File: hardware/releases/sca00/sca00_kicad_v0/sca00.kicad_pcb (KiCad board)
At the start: 2 copper layers, 91.4 x 33 mm, 37 parts, among them J1 Conn_01x13_Pin, J2 Conn_01x03_Pin, J3 Conn_01x06_Pin, J4 Conn_01x03_Pin, J5 Conn_01x01_Pin, J6 Conn_01x01_Pin, SW1 SW_DIP_x02, SW2 SW_DIP_x02, U1 REF6030, U2 ADS8881, U3 SN74LV4051, U4 THS4281

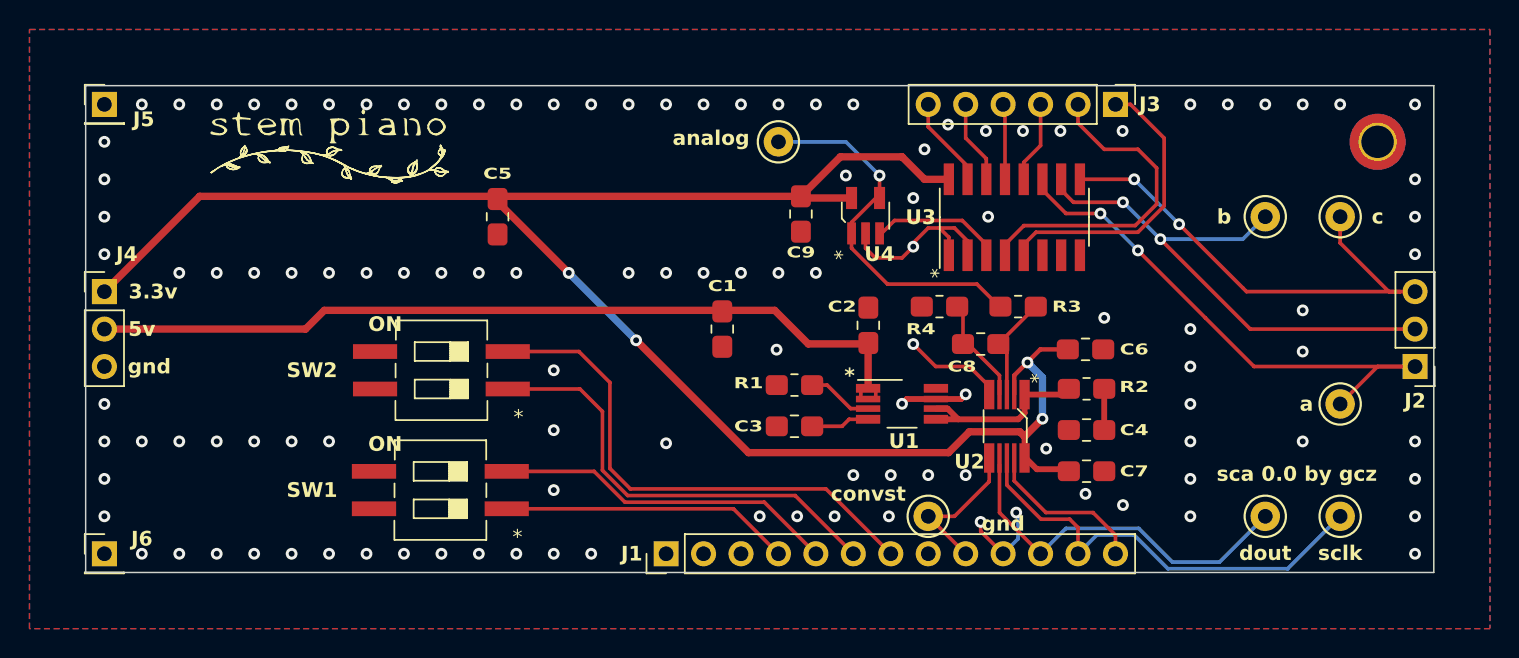
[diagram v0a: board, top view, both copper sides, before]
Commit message: moving connectors for IPS on the bottom of the SCA board, per issue #70
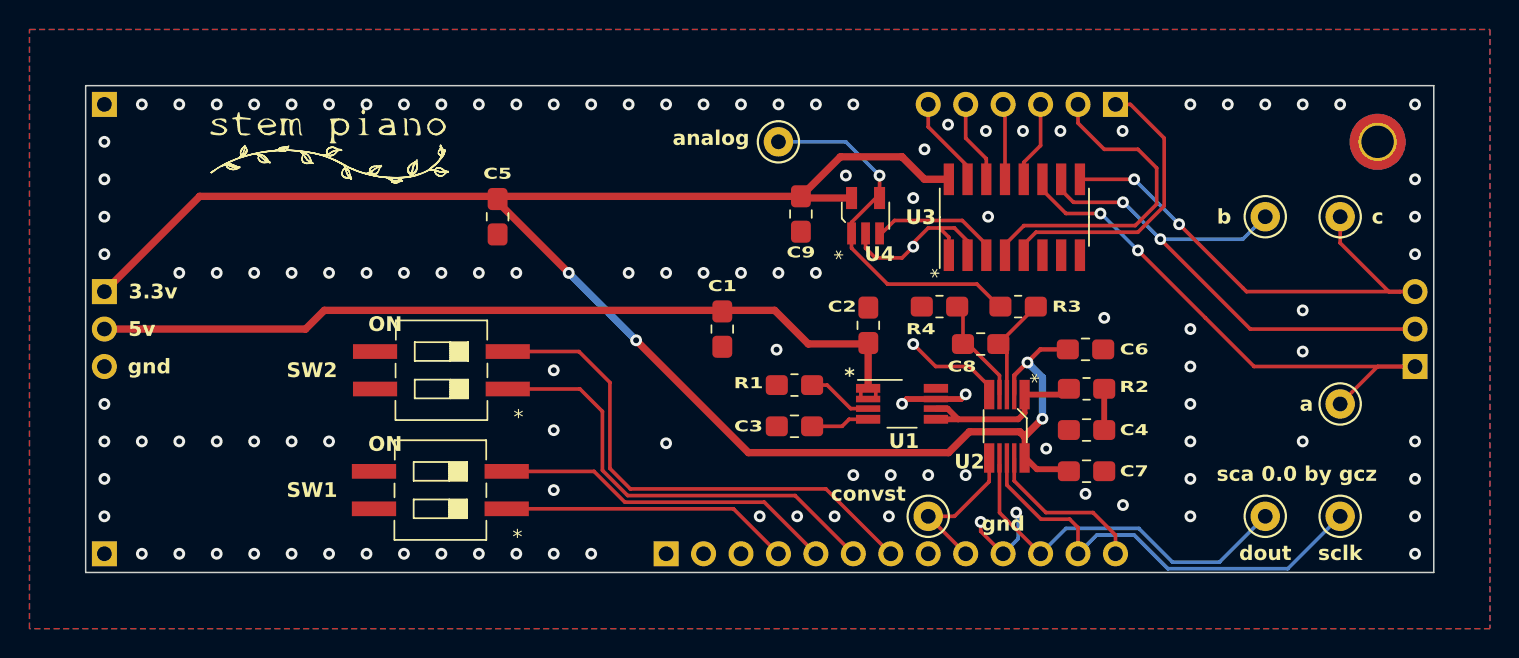
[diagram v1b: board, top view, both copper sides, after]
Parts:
- J1, J2, J3, J4, J5, J6: moved to B.Cu
- turned J1 to -90 degrees
- turned J2 to 0 degrees
- turned J3 to 90 degrees
- turned J4 to 180 degrees
- turned J5 to 180 degrees
- turned J6 to 180 degrees
